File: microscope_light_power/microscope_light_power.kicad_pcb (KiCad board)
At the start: 2 copper layers, 50 x 40 mm, 36 parts, among them IC1 TPS61090, J1 MICROUSB, J2 5V175_out, J3 enable_switch, U1 MCP73871-2AA

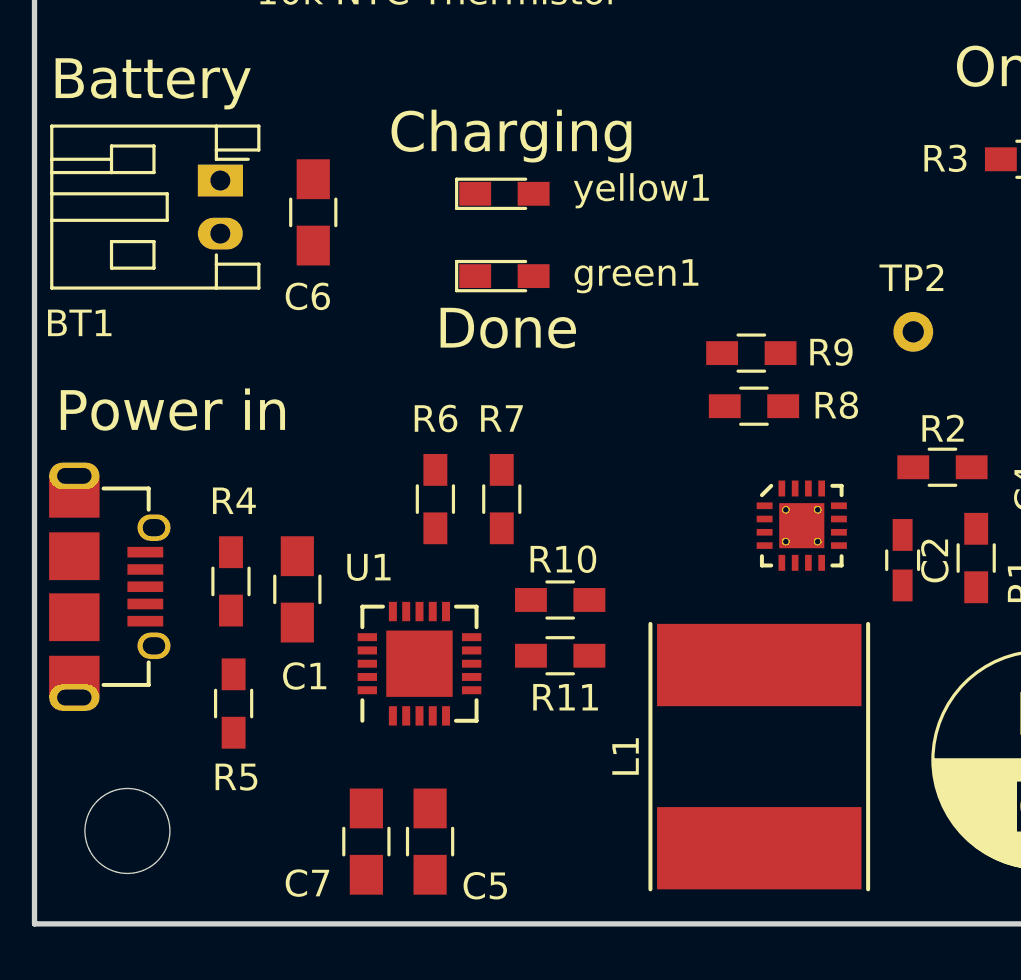
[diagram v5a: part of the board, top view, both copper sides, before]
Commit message: Route the most critical power traces.
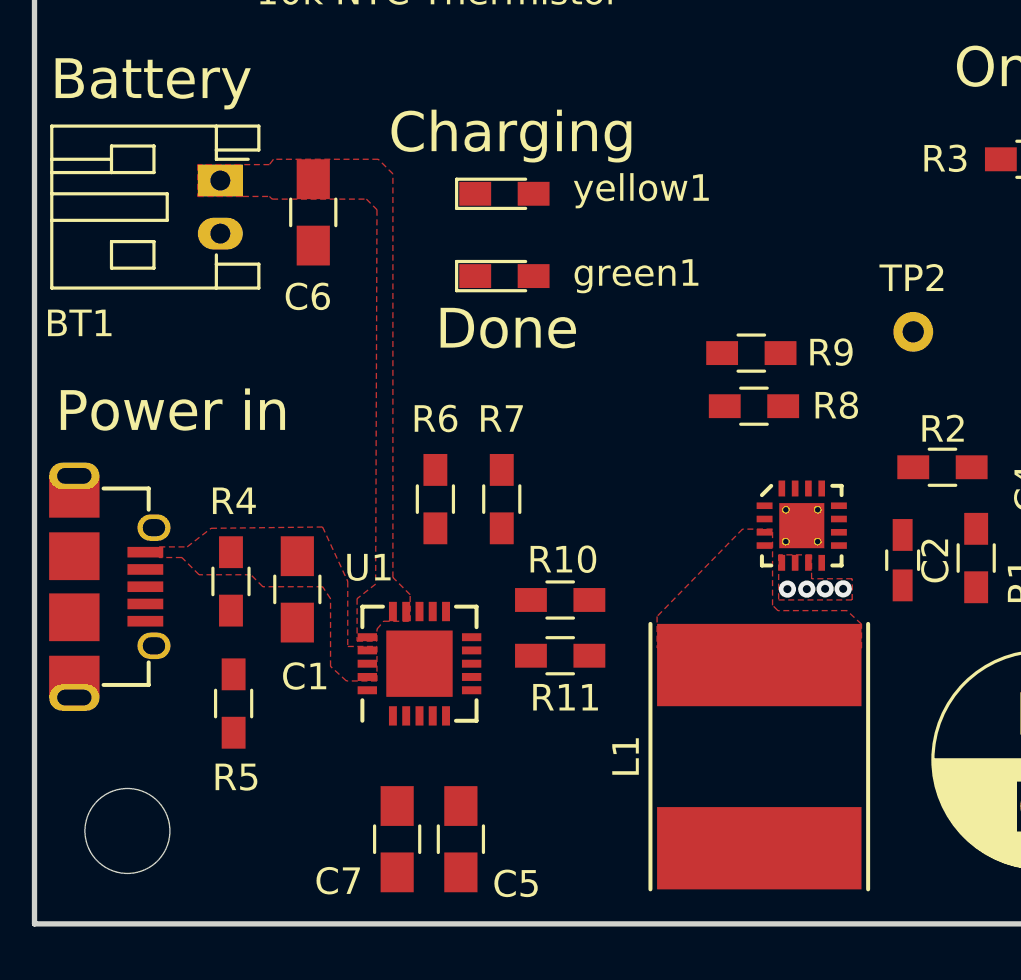
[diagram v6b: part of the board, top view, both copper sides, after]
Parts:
- moved C5 1.16 mm to (116.1, 156.8)
- moved C7 1.16 mm to (113.7, 156.8)
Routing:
- net GND: vias 0 -> 4
- added copper zone on F.Cu, net /SW
- added copper zone on F.Cu, net /Vbat
- added copper zone on F.Cu, net /Vusb
- added copper zone on F.Cu, net GND
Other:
- net class Default: via_dia 0.8 -> 0.65; via_drill 0.4 -> 0.3
- rule pad_to_mask_clearance: 0.2 -> 0.05
- rule via_min_size: 0.4 -> 0.65
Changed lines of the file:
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@@
   (thickness 1.6)
   (drawings 11)
-  (tracks 0)
+  (tracks 4)
   (zones 0)
   (modules 36)
@@
   (thickness 1.6)
   (drawings 11)
-  (tracks 0)
+  (tracks 4)
   (zones 0)
   (modules 36)
@@
 )
 (setup
-  (last_trace_width 0.15)
+  (last_trace_width 0.25)
   (user_trace_width 0.15)
   (user_trace_width 0.3)
@@
   (user_trace_width 0.75)
   (trace_clearance 0.15)
-  (zone_clearance 0.508)
+  (zone_clearance 0.2)
   (zone_45_only no)
   (trace_min 0.15)
   (segment_width 0.2)
   (edge_width 0.15)
-  (via_size 0.8)
-  (via_drill 0.4)
-  (via_min_size 0.4)
+  (via_size 0.65)
+  (via_drill 0.3)
+  (via_min_size 0.65)
   (via_min_drill 0.3)
   (uvia_size 0.3)
@@
   (pad_size 1.524 1.524)
   (pad_drill 0.762)
-  (pad_to_mask_clearance 0.2)
+  (pad_to_mask_clearance 0.05)
   (aux_axis_origin 0 0)
   (visible_elements FFFDFF7F)
@@
   (clearance 0.15)
   (trace_width 0.25)
-  (via_dia 0.8)
-  (via_drill 0.4)
+  (via_dia 0.65)
+  (via_drill 0.3)
   (uvia_dia 0.3)
   (uvia_drill 0.1)
@@
   )
   (module Capacitors_SMD:C_0805_HandSoldering (layer F.Cu)
-    (at 114.9 156.9 270)
+    (at 116.06 156.81 270)
     (descr "Capacitor SMD 0805, hand soldering")
     (tags "capacitor 0805")
@@
   )
   (module Capacitors_SMD:C_0805_HandSoldering (layer F.Cu)
-    (at 112.5 156.9 270)
+    (at 113.66 156.81 270)
     (descr "Capacitor SMD 0805, hand soldering")
     (tags "capacitor 0805")
@@
   (gr_line (start 100 160) (end 150 160) (layer Edge.Cuts) (width 0.2))
   (gr_line (start 100 120) (end 100 160) (layer Edge.Cuts) (width 0.2))
+  (via (at 130.46 147.38) (size 0.65) (drill 0.3) (layers F.Cu B.Cu) (net 6))
+  (via (at 129.78 147.38) (size 0.65) (drill 0.3) (layers F.Cu B.Cu) (net 6))
+  (via (at 129.09 147.39) (size 0.65) (drill 0.3) (layers F.Cu B.Cu) (net 6))
+  (via (at 128.36 147.39) (size 0.65) (drill 0.3) (layers F.Cu B.Cu) (net 6))
+  (zone (net 3) (net_name /Vusb) (layer F.Cu) (hatch edge 0.508)
+    (connect_pads yes (clearance 0.2))
+    (min_thickness 0.2)
+    (fill yes (arc_segments 16) (thermal_gap 0.508) (thermal_bridge_width 0.508))
+    (polygon
+      (pts
+        (xy 104.7 145.8) (xy 105.75 145.8) (xy 106.65 145.1) (xy 110.85 145.05) (xy 111.8 147.1)
+        (xy 111.8 149.55) (xy 112.9 149.55) (xy 112.9 150.85) (xy 111.75 150.85) (xy 111.15 150.3)
+        (xy 111.15 147.75) (xy 110.85 147.3) (xy 108.6 147.3) (xy 108.15 146.85) (xy 106.2 146.85)
+        (xy 105.55 146.2) (xy 104.7 146.2)
+      )
+    )
+  )
+  (zone (net 1) (net_name /Vbat) (layer F.Cu) (hatch edge 0.508)
+    (connect_pads yes (clearance 0.2))
+    (min_thickness 0.2)
+    (fill yes (arc_segments 16) (thermal_gap 0.508) (thermal_bridge_width 0.508))
+    (polygon
+      (pts
+        (xy 114.15 148.6) (xy 114.15 147.6) (xy 113.5 146.95) (xy 113.5 131.75) (xy 112.95 131.2)
+        (xy 109 131.2) (xy 108.85 131.4) (xy 106.15 131.4) (xy 106.15 132.6) (xy 107.85 132.6)
+        (xy 108.85 132.6) (xy 108.95 132.7) (xy 112.5 132.7) (xy 112.9 133.1) (xy 112.85 147.2)
+        (xy 112.15 147.75) (xy 112.15 149.35) (xy 112.9 149.35) (xy 112.9 148.9) (xy 113.15 148.6)
+      )
+    )
+  )
+  (zone (net 23) (net_name /SW) (layer F.Cu) (hatch edge 0.508)
+    (connect_pads yes (clearance 0.2))
+    (min_thickness 0.2)
+    (fill yes (arc_segments 16) (thermal_gap 0.508) (thermal_bridge_width 0.508))
+    (polygon
+      (pts
+        (xy 127.8 145.13) (xy 126.67 145.13) (xy 123.45 148.42) (xy 123.45 149.61) (xy 131.15 149.61)
+        (xy 131.15 148.71) (xy 130.6 148.2) (xy 128 148.2) (xy 127.8 148)
+      )
+    )
+  )
+  (zone (net 6) (net_name GND) (layer F.Cu) (hatch edge 0.508)
+    (connect_pads yes (clearance 0.2))
+    (min_thickness 0.2)
+    (fill yes (arc_segments 16) (thermal_gap 0.508) (thermal_bridge_width 0.508))
+    (polygon
+      (pts
+        (xy 128.03 146.1) (xy 128.03 147.8) (xy 130.8 147.8) (xy 130.8 147) (xy 129.27 147)
+        (xy 129.27 146.1)
+      )
+    )
+  )
 )

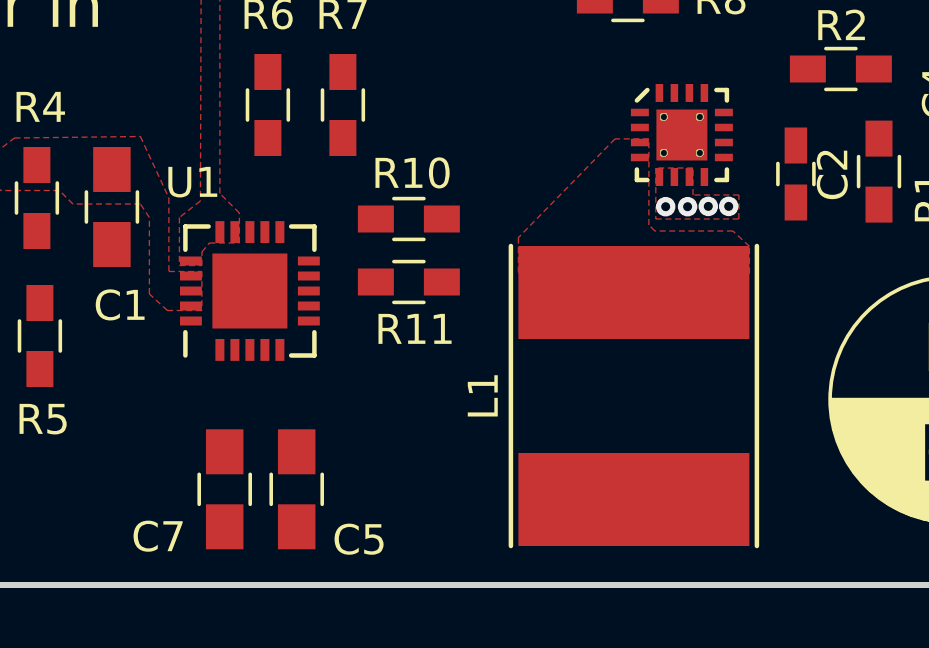
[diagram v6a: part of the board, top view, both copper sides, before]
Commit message: Route some more high current traces.
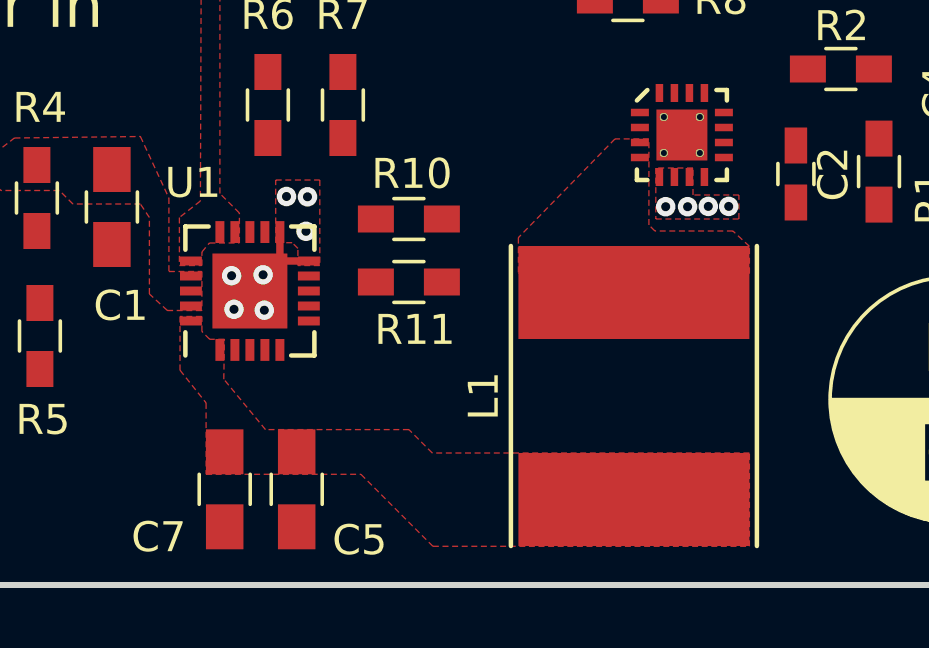
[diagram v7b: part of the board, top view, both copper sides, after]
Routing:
- net GND: track 0.00 -> 2.46 mm, vias 4 -> 11
- added copper zone on F.Cu, net /Vout
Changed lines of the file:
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@@
   (thickness 1.6)
   (drawings 11)
-  (tracks 4)
+  (tracks 14)
   (zones 0)
   (modules 36)
@@
   (thickness 1.6)
   (drawings 11)
-  (tracks 4)
+  (tracks 14)
   (zones 0)
   (modules 36)
@@
   (gr_line (start 100 160) (end 150 160) (layer Edge.Cuts) (width 0.2))
   (gr_line (start 100 120) (end 100 160) (layer Edge.Cuts) (width 0.2))
+  (via (at 113.97 150.81) (size 0.65) (drill 0.3) (layers F.Cu B.Cu) (net 6))
+  (via (at 114.98 150.84) (size 0.65) (drill 0.3) (layers F.Cu B.Cu) (net 6))
+  (via (at 114.94 149.66) (size 0.65) (drill 0.3) (layers F.Cu B.Cu) (net 6))
+  (via (at 113.89 149.69) (size 0.65) (drill 0.3) (layers F.Cu B.Cu) (net 6))
+  (via (at 115.72 147.05) (size 0.65) (drill 0.3) (layers F.Cu B.Cu) (net 6))
+  (via (at 116.42 147.06) (size 0.65) (drill 0.3) (layers F.Cu B.Cu) (net 6))
+  (via (at 116.37 148.21) (size 0.65) (drill 0.3) (layers F.Cu B.Cu) (net 6))
+  (segment (start 116.465 149.2) (end 115.5 149.2) (width 0.25) (layer F.Cu) (net 6))
+  (segment (start 115.5 148.235) (end 115.5 149.2) (width 0.25) (layer F.Cu) (net 6))
+  (segment (start 115.5 149.2) (end 115.125 149.575) (width 0.25) (layer F.Cu) (net 6))
   (via (at 130.46 147.38) (size 0.65) (drill 0.3) (layers F.Cu B.Cu) (net 6))
   (via (at 129.78 147.38) (size 0.65) (drill 0.3) (layers F.Cu B.Cu) (net 6))
@@
       )
     )
+  )
+  (zone (net 2) (net_name /Vout) (layer F.Cu) (hatch edge 0.508)
+    (connect_pads yes (clearance 0.2))
+    (min_thickness 0.2)
+    (fill yes (arc_segments 16) (thermal_gap 0.508) (thermal_bridge_width 0.508))
+    (polygon
+      (pts
+        (xy 112.17 151.05) (xy 112.17 152.84) (xy 113.04 153.93) (xy 113.04 156.31) (xy 118.2 156.31)
+        (xy 120.6 158.71) (xy 131.15 158.71) (xy 131.15 155.6) (xy 120.58 155.6) (xy 119.8 154.82)
+        (xy 115.02 154.82) (xy 113.63 153.14) (xy 113.65 151.81) (xy 113.16 151.81) (xy 112.9 151.55)
+        (xy 112.9 151.05)
+      )
+    )
+  )
+  (zone (net 6) (net_name GND) (layer F.Cu) (hatch edge 0.508)
+    (connect_pads yes (clearance 0.2))
+    (min_thickness 0.2)
+    (fill yes (arc_segments 16) (thermal_gap 0.508) (thermal_bridge_width 0.508))
+    (polygon
+      (pts
+        (xy 115.36 148.59) (xy 115.36 146.5) (xy 116.83 146.5) (xy 116.83 149.35) (xy 116.1 149.35)
+        (xy 116.1 148.78) (xy 115.91 148.59)
+      )
+    )

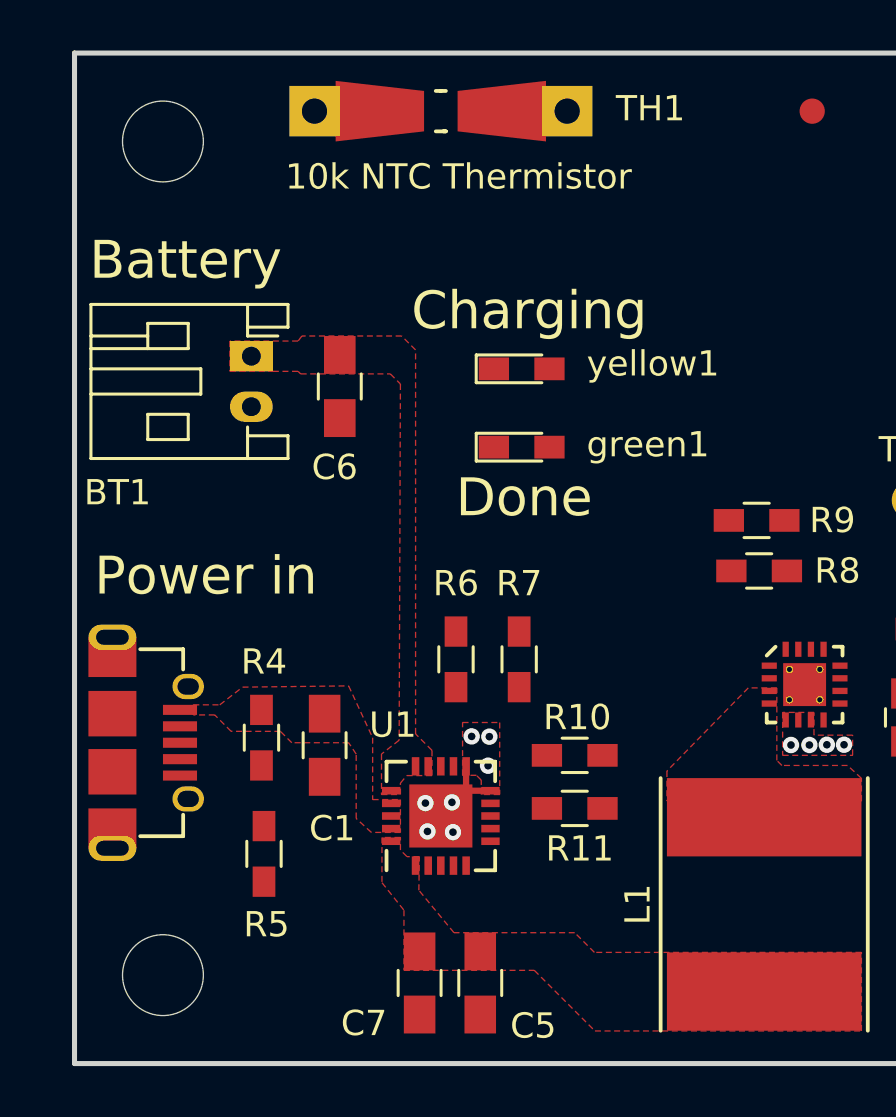
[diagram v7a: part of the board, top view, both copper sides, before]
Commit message: Routed all of the direct connections from the MCP73871. I also added a note about the very bizarre routing for the thermistor. By the time I realized its trace would have to go on the bottom a good chunk of this board was routed. I routed it along the outside of the board to prevent breaking up the ground plane.
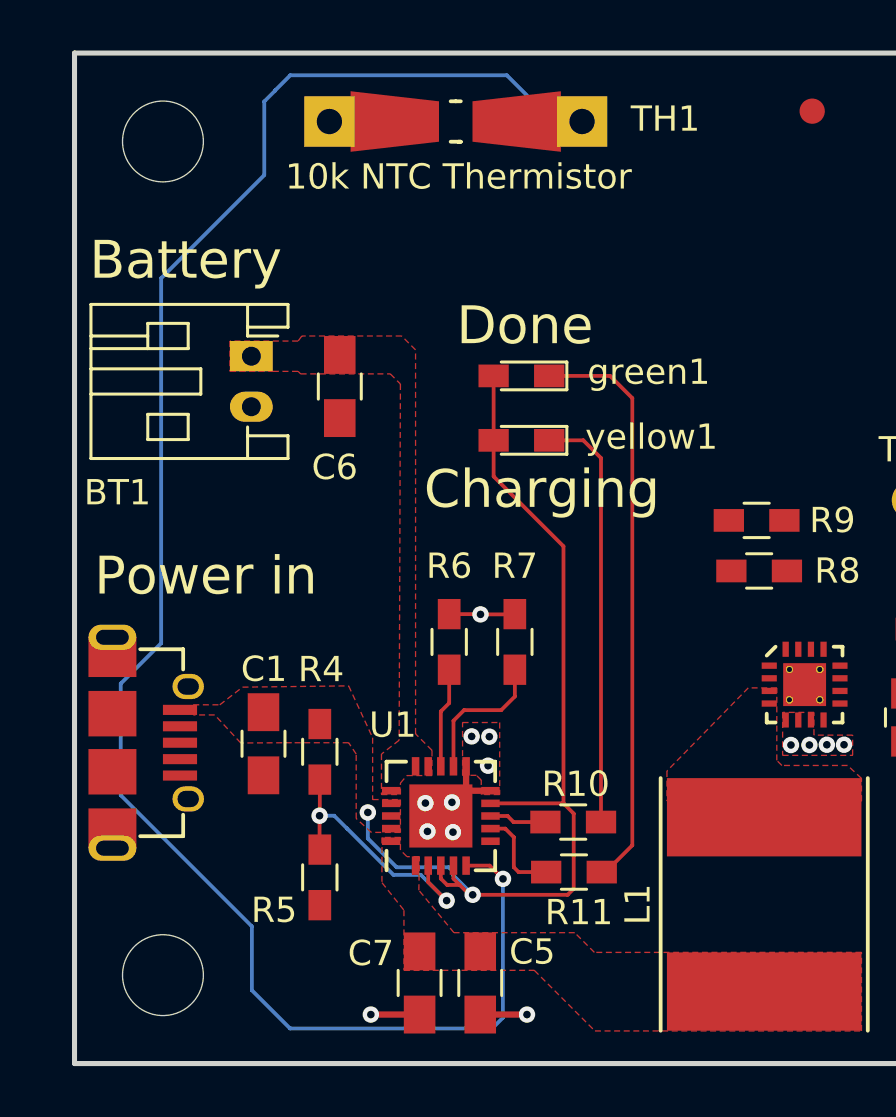
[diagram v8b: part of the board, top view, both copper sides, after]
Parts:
- moved yellow1 2.83 mm to (117.7, 135.3), turned to 180 degrees
- moved green1 2.82 mm to (117.7, 132.8), turned to 180 degrees
- moved R10 2.64 mm to (119.7, 150.4)
- moved R11 2.52 mm to (119.8, 152.4)
- moved C1 2.42 mm to (107.5, 147.3)
- moved R5 2.40 mm to (109.7, 152.6)
- moved R4 2.38 mm to (109.7, 147.7)
- moved R6 0.74 mm to (114.8, 143.3)
- moved TH1 0.72 mm to (115.1, 122.7)
- moved R7 0.71 mm to (117.4, 143.3)
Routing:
- net Net-(TH1-Pad1): track 0.00 -> 71.4 mm, vias 0 -> 1
- net /Vusb: track 0.00 -> 37.7 mm, vias 0 -> 2
- net Net-(R11-Pad1): track 0.00 -> 23.0 mm
- net Net-(R10-Pad1): track 0.00 -> 16.7 mm
- net Net-(R4-Pad1): track 0.00 -> 10.9 mm, vias 0 -> 2
- net GND: track 2.46 -> 8.85 mm, vias 11 -> 14
- net Net-(R7-Pad1): track 0.00 -> 5.69 mm
- net Net-(R6-Pad1): track 0.00 -> 3.96 mm
- net Net-(R11-Pad2): track 0.00 -> 3.61 mm
- net Net-(R10-Pad2): track 0.00 -> 2.27 mm
